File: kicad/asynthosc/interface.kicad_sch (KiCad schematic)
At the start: 22 parts, among them SW6 RotaryEncoder_Switch, SW7 SW_MEC_5G_LED, SW8 SW_MEC_5G_LED

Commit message: sch: alternative displays. pcb: wip
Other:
- note added: "Alternatives to:"
- note added: "Smaller:"
- note added: "X154-2864KSWBG01-C24"
- note added: "X223-2832ALBCG02-C24"
- note added: "X242-2864KLBUG01-C24"
- note added: "X242-2864KSYUG01-C24"
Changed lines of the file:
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@@
+		)
+	)
+	(text "X242-2864KLBUG01-C24"
+		(exclude_from_sim no)
+		(at 215.9 117.348 0)
+		(effects
+			(font
+				(size 1.27 1.27)
+			)
 		)
 	)
@@
 		)
 	)
+	(text "Smaller:"
+		(exclude_from_sim no)
+		(at 208.026 124.714 0)
+		(effects
+			(font
+				(size 1.27 1.27)
+			)
+		)
+	)
+	(text "X154-2864KSWBG01-C24  "
+		(exclude_from_sim no)
+		(at 217.17 110.998 0)
+		(effects
+			(font
+				(size 1.27 1.27)
+			)
+		)
+	)
 	(text "Alps EC11E18244AU"
 		(exclude_from_sim no)
 		(at 64.516 104.902 0)
+		(effects
+			(font
+				(size 1.27 1.27)
+			)
+		)
+	)
+	(text "X242-2864KSYUG01-C24"
+		(exclude_from_sim no)
+		(at 215.9 120.142 0)
+		(effects
+			(font
+				(size 1.27 1.27)
+			)
+		)
+	)
+	(text "X223-2832ALBCG02-C24 "
+		(exclude_from_sim no)
+		(at 216.662 127.508 0)
 		(effects
 			(font
@@
 		(effects
 			(font
+				(size 1.27 1.27)
+			)
+		)
+	)
+	(text "Alternatives to:"
+		(exclude_from_sim no)
+		(at 211.074 108.204 0)
+		(effects
+			(font

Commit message: bom: update mfr, serials and lcsc fields
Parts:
- DS1: LCSC (none) -> C22360346
- DS1_S1: LCSC (none) -> C5123567
- SW6: LCSC (none) -> C202365
- SW7, SW8: LCSC (none) -> C2762115
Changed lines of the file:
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@@
 			)
 		)
-		(property "LCSC" ""
+		(property "LCSC" "C22360346"
 			(at 182.88 93.98 0)
 			(effects
@@
 			)
 		)
+		(property "LCSC" "C202365"
+			(at 59.69 125.73 0)
+			(effects
+				(font
+					(size 1.27 1.27)
+				)
+				(hide yes)
+			)
+		)
 		(pin "B"
 		)
@@
 			)
 		)
-		(property "LCSC" ""
+		(property "LCSC" "C5123567"
 			(at 200.66 101.6 0)
 			(effects
@@
 			)
 		)
-		(property "LCSC" ""
+		(property "LCSC" "C2762115"
 			(at 60.96 74.93 0)
 			(effects
@@
 			)
 		)
-		(property "LCSC" ""
+		(property "LCSC" "C2762115"
 			(at 62.23 176.53 0)
 			(effects

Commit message: bom: sch: pcb: update for sourcing in jlc pcba services
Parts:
- DS1: footprint asynthosc:HRO_FPC0.5B-WTG-24P_1x24-1MP_P0.5mm_Horizontal -> asynthosc:Hirose_FH52-24S-0.5SH_1x24-1MP_P0.5mm_Horizontal; LCSC C22360346 -> C5378714; Manufacturer HRO Parts -> Hirose; RefNum FPC0.5B-WTG-24P -> FH52-24S-0.5SH
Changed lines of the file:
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@@
 			)
 		)
-		(property "Footprint" "asynthosc:HRO_FPC0.5B-WTG-24P_1x24-1MP_P0.5mm_Horizontal"
+		(property "Footprint" "asynthosc:Hirose_FH52-24S-0.5SH_1x24-1MP_P0.5mm_Horizontal"
 			(at 183.642 96.774 0)
 			(effects
@@
 			)
 		)
-		(property "LCSC" "C22360346"
+		(property "LCSC" "C5378714"
 			(at 182.88 93.98 0)
 			(effects
@@
 			)
 		)
-		(property "Manufacturer" "HRO Parts"
+		(property "Manufacturer" "Hirose"
 			(at 182.88 93.98 0)
 			(effects
@@
 			)
 		)
-		(property "RefNum" "FPC0.5B-WTG-24P "
+		(property "RefNum" "FH52-24S-0.5SH"
 			(at 182.88 93.98 0)
 			(effects

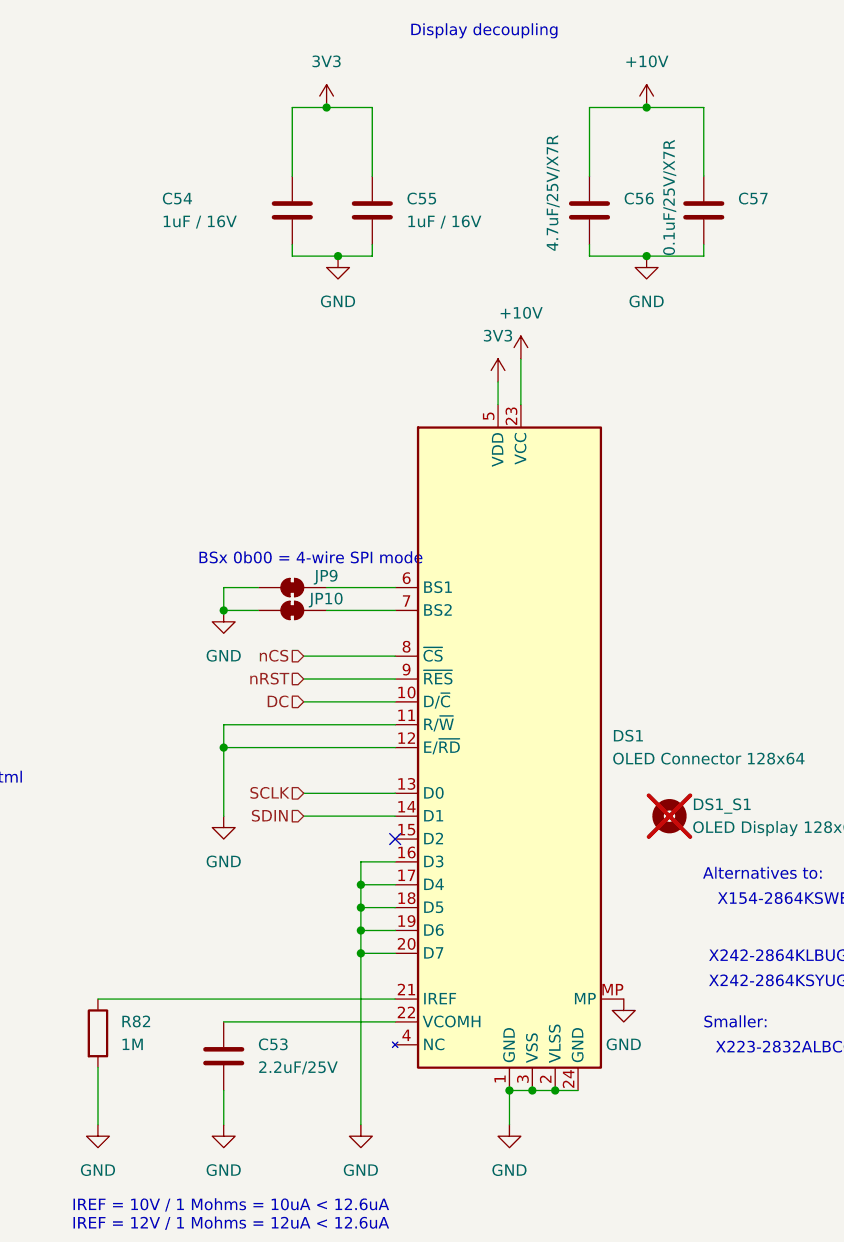
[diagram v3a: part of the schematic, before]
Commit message: bom: update for better bom
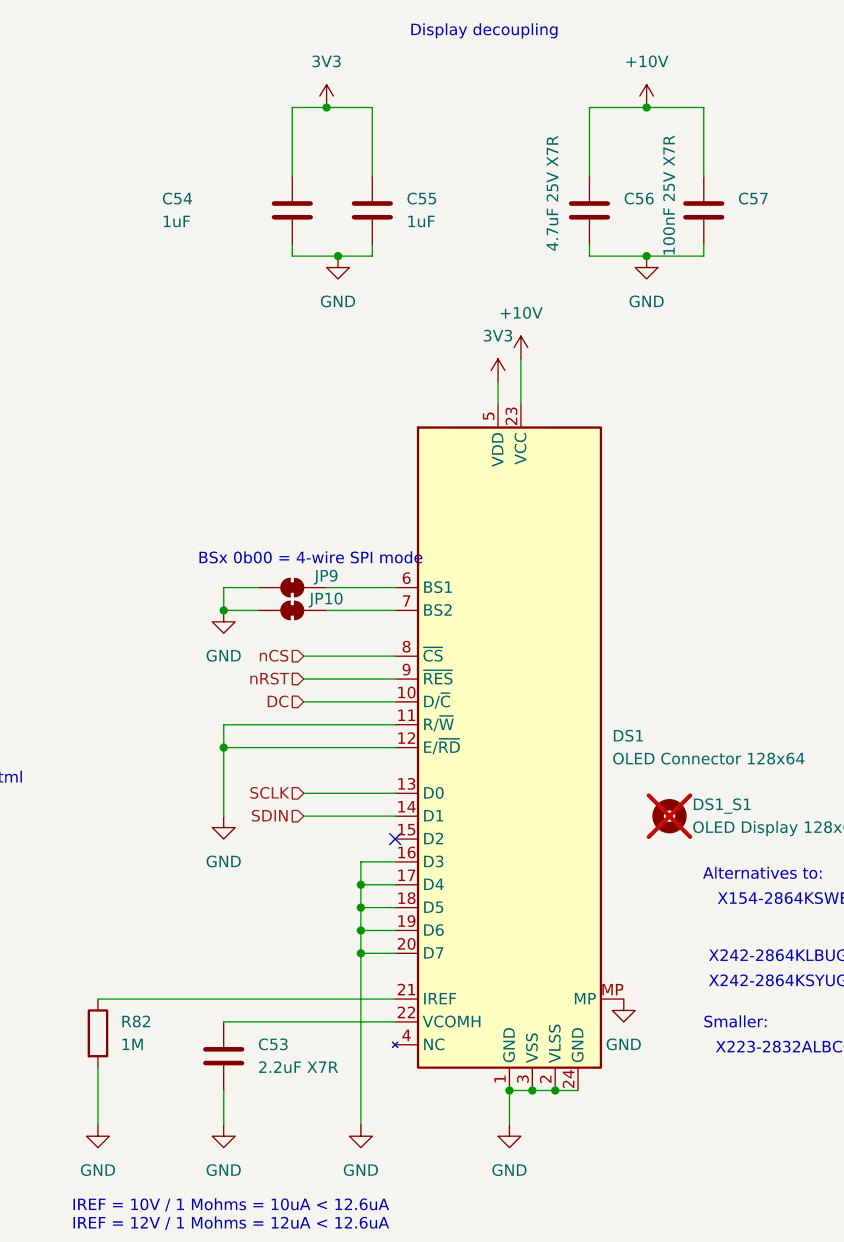
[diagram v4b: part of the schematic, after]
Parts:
- C53: value 2.2uF/25V -> 2.2uF X7R
- C54, C55: value 1uF / 16V -> 1uF
- C56: value 4.7uF/25V/X7R -> 4.7uF 25V X7R
- C57: value 0.1uF/25V/X7R -> 100nF 25V X7R
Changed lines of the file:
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@@
 			)
 		)
-		(property "Value" "4.7uF/25V/X7R"
+		(property "Value" "4.7uF 25V X7R"
 			(at 187.706 38.862 90)
 			(effects
@@
 			)
 		)
-		(property "Value" "0.1uF/25V/X7R"
+		(property "Value" "100nF 25V X7R"
 			(at 200.66 39.37 90)
 			(effects
@@
 			)
 		)
-		(property "Value" "1uF / 16V"
+		(property "Value" "1uF"
 			(at 171.45 35.5599 0)
 			(effects
@@
 			)
 		)
-		(property "Value" "2.2uF/25V"
+		(property "Value" "2.2uF X7R"
 			(at 154.94 129.5399 0)
 			(effects
@@
 			)
 		)
-		(property "Value" "1uF / 16V"
+		(property "Value" "1uF"
 			(at 144.272 35.56 0)
 			(effects

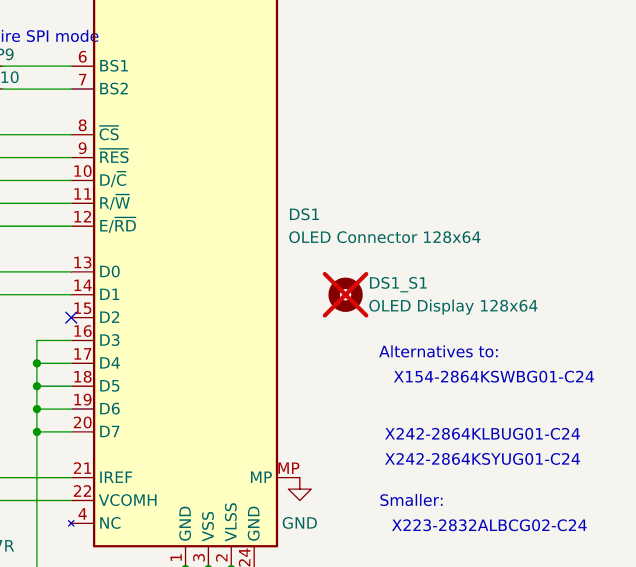
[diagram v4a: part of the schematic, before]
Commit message: bom: add jlcpcb field with simplified footprint
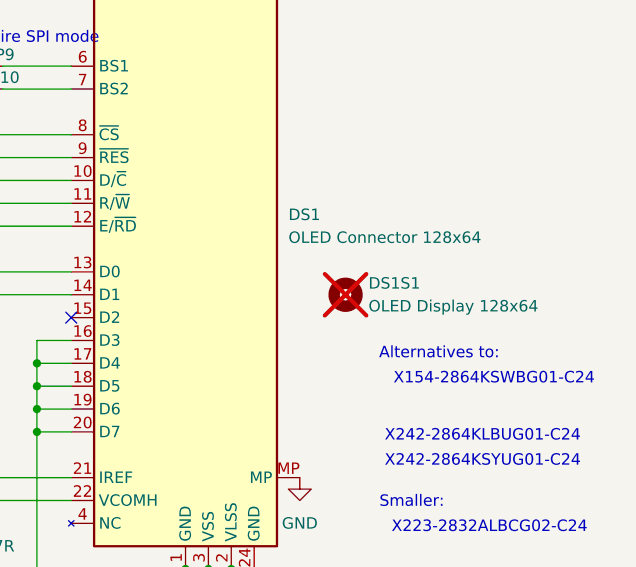
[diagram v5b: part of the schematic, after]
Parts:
- C51, C52, R76, R77, R78, R79, R80, R81, R82, R84: JLC (none) -> 0402
- C53, C54, C55, C56, C57: JLC (none) -> 0805
- renumbered DS1_S1 to DS1S1
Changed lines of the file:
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@@
 			)
 		)
+		(property "JLC" "0805"
+			(at 191.77 34.29 0)
+			(effects
+				(font
+					(size 1.27 1.27)
+				)
+				(hide yes)
+			)
+		)
 		(pin "1"
 		)
@@
 			)
 		)
+		(property "JLC" "0402"
+			(at 36.83 134.62 0)
+			(effects
+				(font
+					(size 1.27 1.27)
+				)
+				(hide yes)
+			)
+		)
 		(pin "2"
 		)
@@
 			)
 		)
+		(property "JLC" ""
+			(at 182.88 93.98 0)
+			(effects
+				(font
+					(size 1.27 1.27)
+				)
+				(hide yes)
+			)
+		)
 		(pin "9"
 		)
@@
 			)
 		)
+		(property "JLC" ""
+			(at 59.69 125.73 0)
+			(effects
+				(font
+					(size 1.27 1.27)
+				)
+				(hide yes)
+			)
+		)
 		(pin "B"
 		)
@@
 			)
 		)
+		(property "JLC" "0805"
+			(at 204.47 34.29 0)
+			(effects
+				(font
+					(size 1.27 1.27)
+				)
+				(hide yes)
+			)
+		)
 		(pin "1"
 		)
@@
 			)
 		)
+		(property "JLC" "0805"
+			(at 167.64 34.29 0)
+			(effects
+				(font
+					(size 1.27 1.27)
+				)
+				(hide yes)
+			)
+		)
 		(pin "2"
 		)
@@
 			)
 		)
+		(property "JLC" "0402"
+			(at 50.8 67.31 0)
+			(effects
+				(font
+					(size 1.27 1.27)
+				)
+				(hide yes)
+			)
+		)
 		(pin "1"
 		)
@@
 			)
 		)
+		(property "JLC" "0805"
+			(at 151.13 128.27 0)
+			(effects
+				(font
+					(size 1.27 1.27)
+				)
+				(hide yes)
+			)
+		)
 		(pin "1"
 		)
@@
 		(dnp yes)
 		(fields_autoplaced yes)
-		(property "Reference" "DS1_S1"
+		(property "Reference" "DS1S1"
 			(at 203.2 100.3299 0)
 			(effects
@@
 			)
 		)
+		(property "JLC" ""
+			(at 200.66 101.6 0)
+			(effects
+				(font
+					(size 1.27 1.27)
+				)
+				(hide yes)
+			)
+		)
 		(instances
 			(project "asynthosc"
 				(path "/d73e377a-a016-415f-8824-91cc6e4907b9/b863f609-74bc-4dca-9f89-b76b25b90e2d"
-					(reference "DS1_S1")
+					(reference "DS1S1")
 					(unit 1)
 				)
@@
 			)
 		)
+		(property "JLC" "0402"
+			(at 36.83 114.3 0)
+			(effects
+				(font
+					(size 1.27 1.27)
+				)
+				(hide yes)
+			)
+		)
 		(pin "1"
 		)
@@
 			)
 		)
+		(property "JLC" ""
+			(at 60.96 74.93 0)
+			(effects
+				(font
+					(size 1.27 1.27)
+				)
+				(hide yes)
+			)
+		)
 		(pin "3"
 		)
@@
 			)
 		)
+		(property "JLC" "0402"
+			(at 44.45 114.3 0)
+			(effects
+				(font
+					(size 1.27 1.27)
+				)
+				(hide yes)
+			)
+		)
 		(pin "1"
 		)
@@
 			)
 		)
+		(property "JLC" "0402"
+			(at 78.74 134.62 0)
+			(effects
+				(font
+					(size 1.27 1.27)
+				)
+				(hide yes)
+			)
+		)
 		(pin "1"
 		)
@@
 			)
 		)
+		(property "JLC" "0402"
+			(at 78.74 176.53 0)
+			(effects
+				(font
+					(size 1.27 1.27)
+				)
+				(hide yes)
+			)
+		)
 		(pin "1"
 		)
@@
 			)
 		)
+		(property "JLC" "0402"
+			(at 52.07 168.91 0)
+			(effects
+				(font
+					(size 1.27 1.27)
+				)
+				(hide yes)
+			)
+		)
 		(pin "1"
 		)
@@
 			)
 		)
+		(property "JLC" "0402"
+			(at 137.16 125.73 0)
+			(effects
+				(font
+					(size 1.27 1.27)
+				)
+				(hide yes)
+			)
+		)
 		(pin "1"
 		)
@@
 			)
 		)
+		(property "JLC" "0805"
+			(at 158.75 34.29 0)
+			(effects
+				(font
+					(size 1.27 1.27)
+				)
+				(hide yes)
+			)
+		)
 		(pin "2"
 		)
@@
 			)
 		)
+		(property "JLC" "0402"
+			(at 44.45 134.62 0)
+			(effects
+				(font
+					(size 1.27 1.27)
+				)
+				(hide yes)
+			)
+		)
 		(pin "2"
 		)
@@
 			)
 		)
+		(property "JLC" ""
+			(at 158.75 76.2 0)
+			(effects
+				(font
+					(size 1.27 1.27)
+				)
+				(hide yes)
+			)
+		)
 		(pin "2"
 		)
@@
 			)
 		)
+		(property "JLC" ""
+			(at 158.75 78.74 0)
+			(effects
+				(font
+					(size 1.27 1.27)
+				)
+				(hide yes)
+			)
+		)
 		(pin "2"
 		)
@@
 			)
 		)
+		(property "JLC" ""
+			(at 62.23 176.53 0)
+			(effects
+				(font
+					(size 1.27 1.27)
+				)
+				(hide yes)
+			)
+		)
 		(pin "3"
 		)
@@
 			(at 77.47 74.93 0)
 			(effects
+				(font
+					(size 1.27 1.27)
+				)
+				(hide yes)
+			)
+		)
+		(property "JLC" "0402"
+			(at 77.47 74.93 0)
+			(effects

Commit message: pcb: bom: comp: misc fixes, button footprint, and move usb-b away from rj45
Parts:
- SW6: LCSC C202365 -> C370986; RefNum EC11E18244AU -> EC11E18
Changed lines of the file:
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@@
 			)
 		)
-		(property "RefNum" "EC11E18244AU"
+		(property "RefNum" "EC11E18"
 			(at 59.69 125.73 0)
 			(effects
@@
 			)
 		)
-		(property "LCSC" "C202365"
+		(property "LCSC" "C370986"
 			(at 59.69 125.73 0)
 			(effects

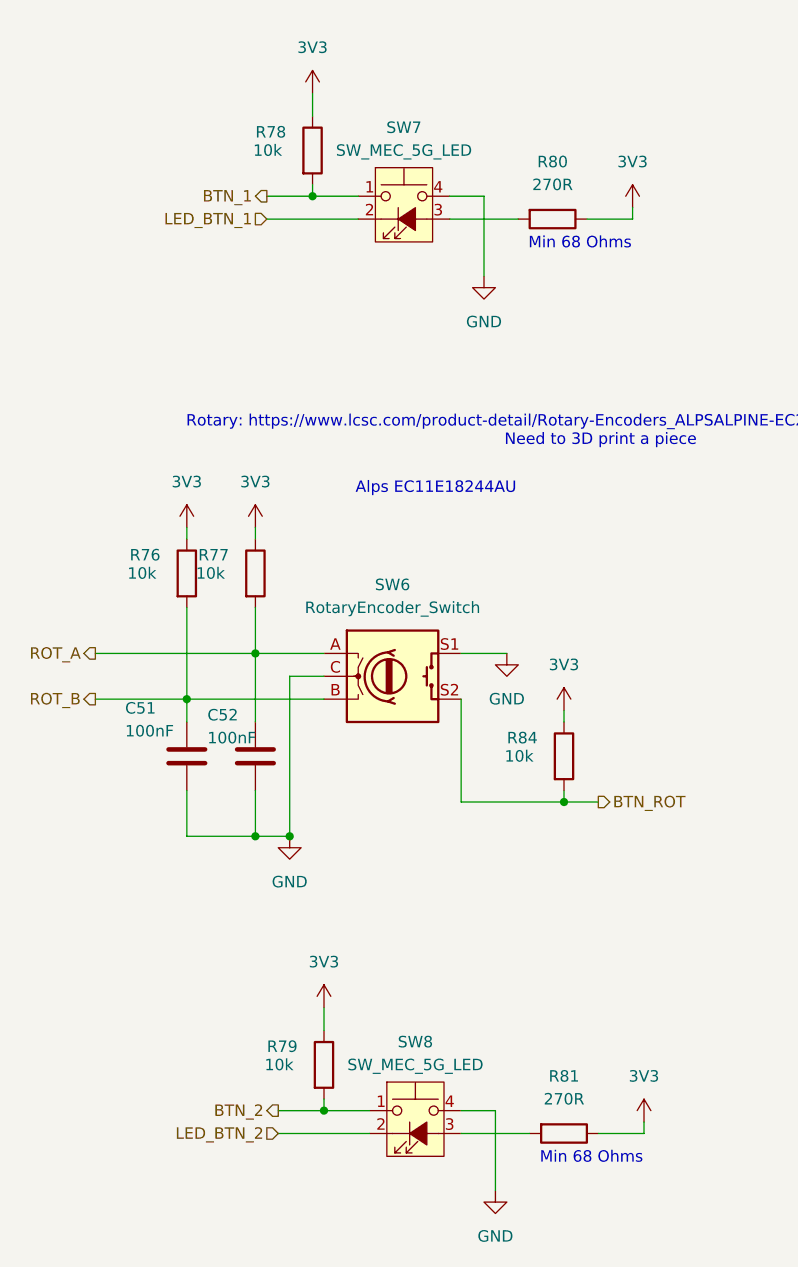
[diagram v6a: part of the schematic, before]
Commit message: bom: dnp for all manually equiped components
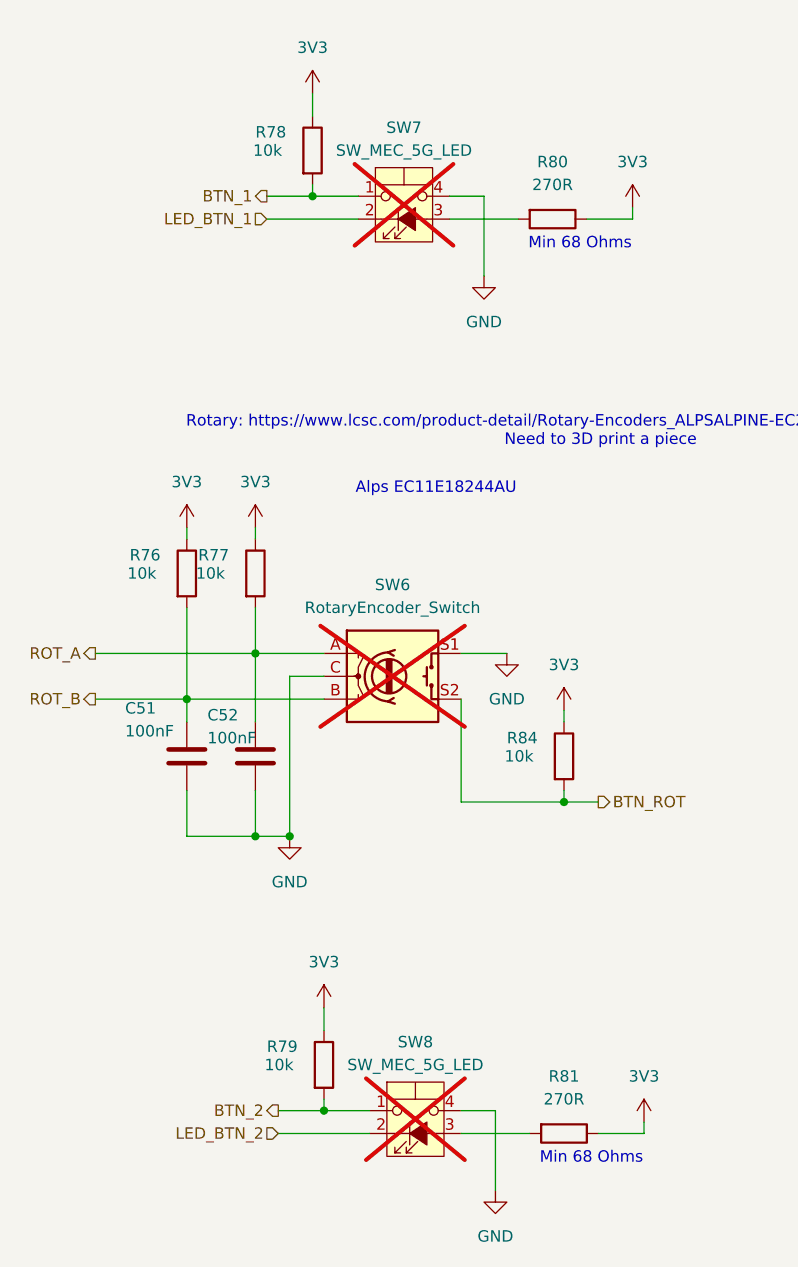
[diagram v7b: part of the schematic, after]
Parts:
- SW6, SW7, SW8: now not fitted
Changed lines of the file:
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@@
 		(in_bom yes)
 		(on_board yes)
-		(dnp no)
+		(dnp yes)
 		(fields_autoplaced yes)
 		(property "Reference" "SW6"
@@
 		(in_bom yes)
 		(on_board yes)
-		(dnp no)
+		(dnp yes)
 		(fields_autoplaced yes)
 		(property "Reference" "SW7"
@@
 		(in_bom yes)
 		(on_board yes)
-		(dnp no)
+		(dnp yes)
 		(fields_autoplaced yes)
 		(property "Reference" "SW8"

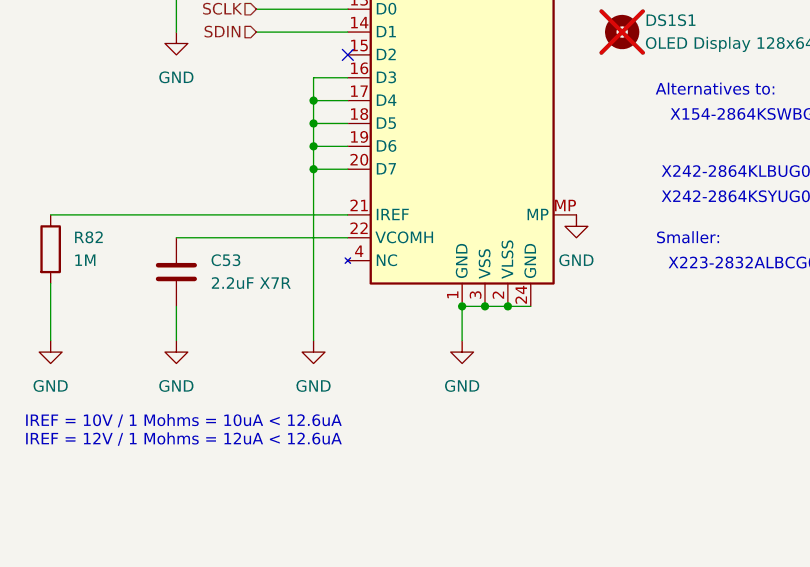
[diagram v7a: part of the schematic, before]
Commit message: sch: nc to gnd
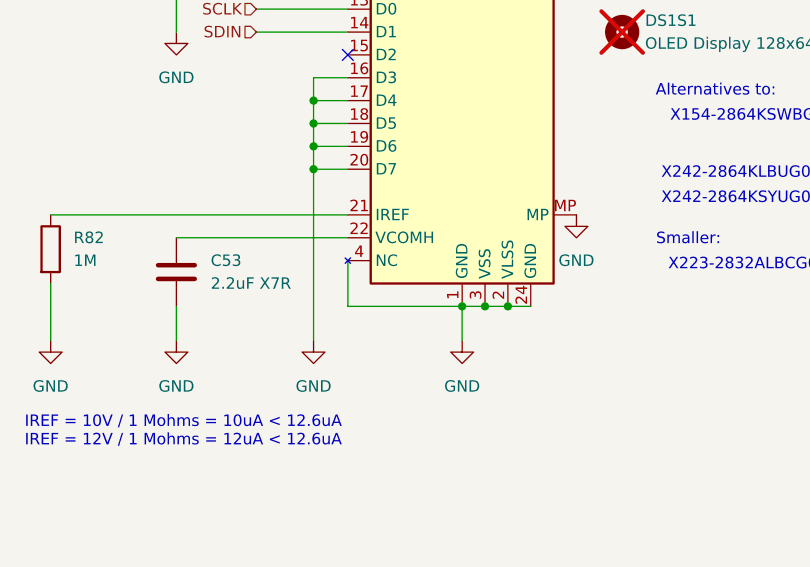
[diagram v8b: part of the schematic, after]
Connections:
- net GND: now also DS1.4 (NC)
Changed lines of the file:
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@@
+	(wire
+		(pts
+			(xy 170.18 132.08) (xy 182.88 132.08)
+		)
+		(stroke
+			(width 0)
+			(type default)
+		)
+	)
 	(wire
 		(pts
@@
 		)
 		(stroke
+			(width 0)
+			(type default)
+		)
+	)
+	(wire
+		(pts
+			(xy 170.18 127) (xy 170.18 132.08)
+		)
+		(stroke
